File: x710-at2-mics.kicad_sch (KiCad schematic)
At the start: 1 part, among them U1 EZX710AT2_S_LMR5

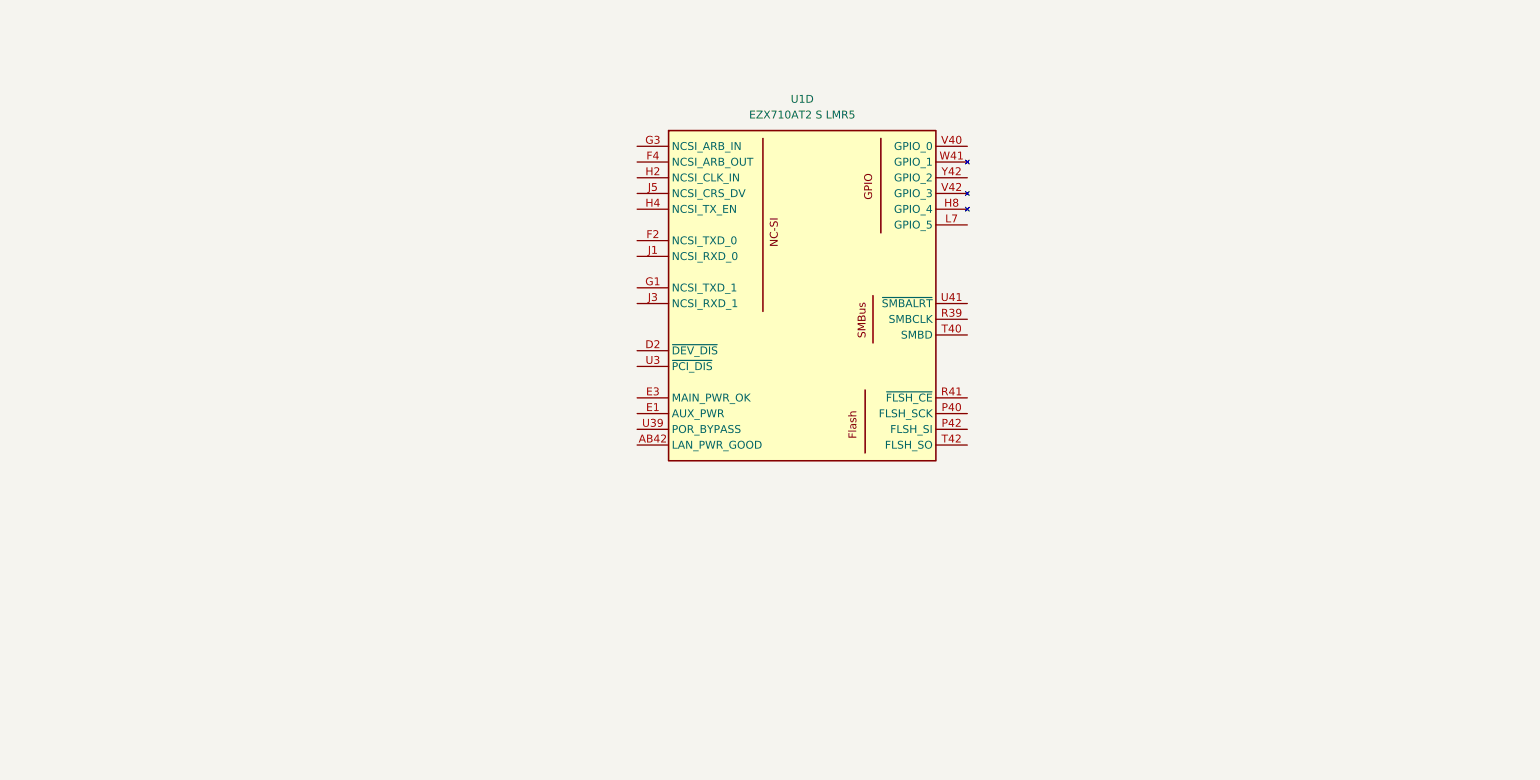
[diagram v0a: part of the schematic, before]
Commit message: [#80813] Add RJ45 connectors, add SMBus, FLASH SPI and misc
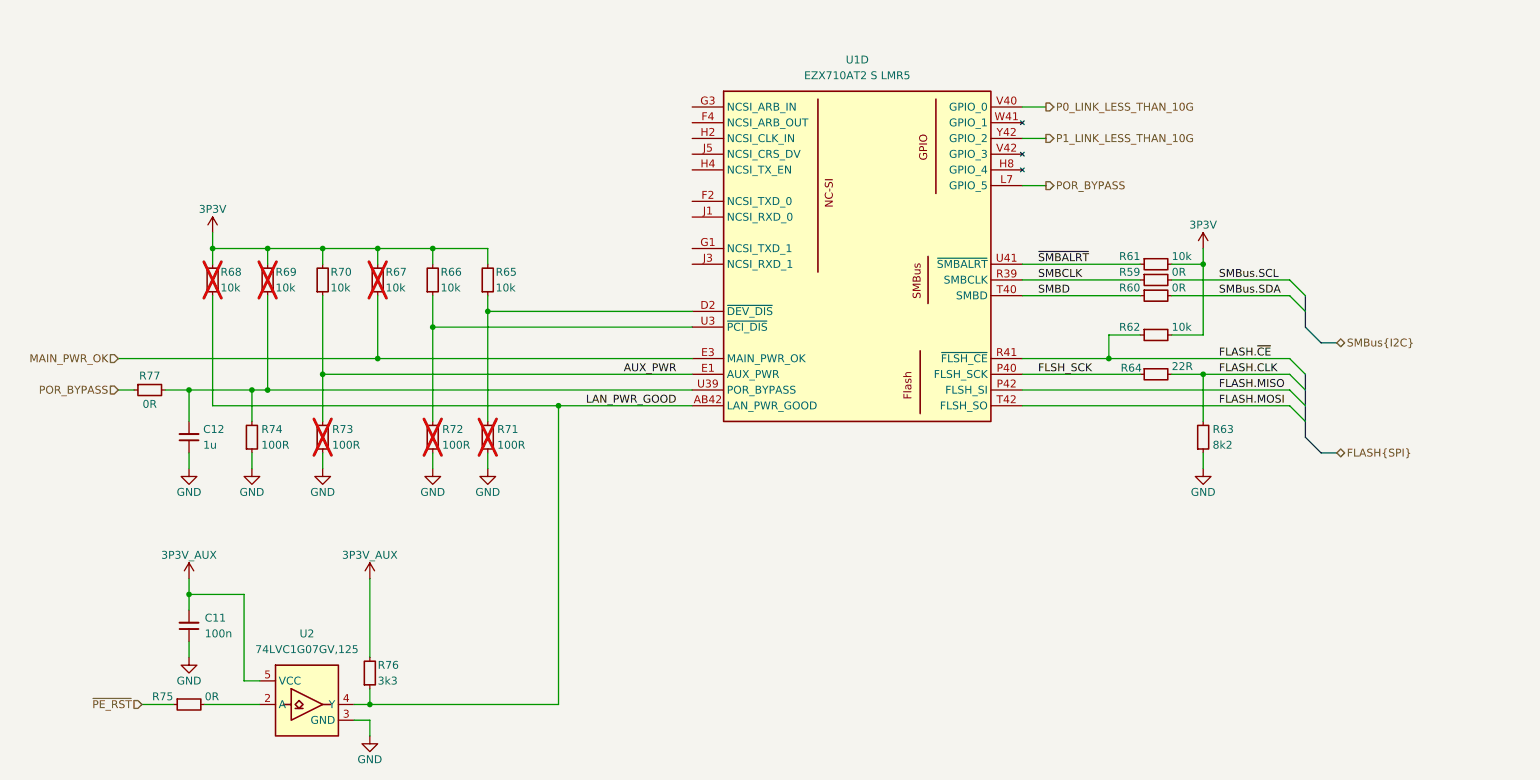
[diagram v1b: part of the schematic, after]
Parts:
- added C11: C_100n_16V_X7R_0402, antmicro-footprints:C_0402_1005Metric, symbol antmicroCapacitors0402:C_100n_16V_X7R_0402
- added C12: C_1u_16V_X7R_0603, antmicro-footprints:C_0603_1608Metric, symbol antmicroCapacitors0603:C_1u_16V_X7R_0603
- added R59, R60, R75, R77: R_0R_0402, antmicro-footprints:R_0402_1005Metric, symbol antmicroResistors0402:R_0R_0402
- added R61, R62, R65, R66, R67, R68, R69, R70: R_10k_0402, antmicro-footprints:R_0402_1005Metric, symbol antmicroResistors0402:R_10k_0402
- added R63: R_8k2_0402, antmicro-footprints:R_0402_1005Metric, symbol antmicroResistors0402:R_8k2_0402
- added R64: R_22R_0402, antmicro-footprints:R_0402_1005Metric, symbol antmicroResistors0402:R_22R_0402
- added R71, R72, R73, R74: R_100R_0402, antmicro-footprints:R_0402_1005Metric, symbol antmicroResistors0402:R_100R_0402
- added R76: R_3k3_0402, antmicro-footprints:R_0402_1005Metric, symbol antmicroResistors0402:R_3k3_0402
- added unit 6 of U1
- added U2: 74LVC1G07_SOT-753, antmicro-footprints:SOT-753, symbol antmicroLogicBuffersDriversReceiversTransceivers:74LVC1G07_SOT-753
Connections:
- net LAN_PWR_GOOD: now reaches U1.AB42 (LAN_PWR_GOOD)
- net LAN_PWR_GOOD: now also R68.1, R76.1, U2.4 (Y)
- net at U1.D2 (~{DEV_DIS}): now also R65.1, R71.2
- net AUX_PWR: now reaches U1.E1 (AUX_PWR)
- net AUX_PWR: now also R70.1, R73.2
- net MAIN_PWR_OK: now reaches U1.E3 (MAIN_PWR_OK)
- net MAIN_PWR_OK: now also R67.1
- net POR_BYPASS: now reaches U1.L7 (GPIO_5)
- net POR_BYPASS: now also R77.1
- net FLSH_SCK: now reaches U1.P40 (FLSH_SCK)
- net FLSH_SCK: now also R64.1
- net FLASH.MISO: now reaches U1.P42 (FLSH_SI)
- net SMBCLK: now reaches U1.R39 (SMBCLK)
- net SMBCLK: now also R59.1
- net FLASH.~{CE}: now reaches U1.R41 (~{FLSH_CE})
- net FLASH.~{CE}: now also R62.1
- net SMBD: now reaches U1.T40 (SMBD)
- net SMBD: now also R60.1
- net FLASH.MOSI: now reaches U1.T42 (FLSH_SO)
- net at U1.U3 (~{PCI_DIS}): now also R66.1, R72.2
- net at U1.U39 (POR_BYPASS): now also C12.2, R69.1, R74.2, R77.2
- net ~{SMBALRT}: now reaches U1.U41 (~{SMBALRT})
- net ~{SMBALRT}: now also R61.1
- net P0_LINK_LESS_THAN_10G: now reaches U1.V40 (GPIO_0)
- net P1_LINK_LESS_THAN_10G: now reaches U1.Y42 (GPIO_2)
- new net: R75.2, U2.2 (A)
- new net 3P3V: R61.2, R62.2, R65.2, R66.2, R67.2, R68.2, R69.2, R70.2
- new net 3P3V_AUX: C11.2, R76.2, U2.5 (VCC)
- new net FLASH.CLK: R63.2, R64.2
- new net GND: C11.1, C12.1, R63.1, R71.1, R72.1, R73.1, R74.1, U2.3 (GND)
- new net SMBus.SCL: R59.2
- new net SMBus.SDA: R60.2
- new net ~{PE_RST}: R75.1
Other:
- moved on the sheet: U1D

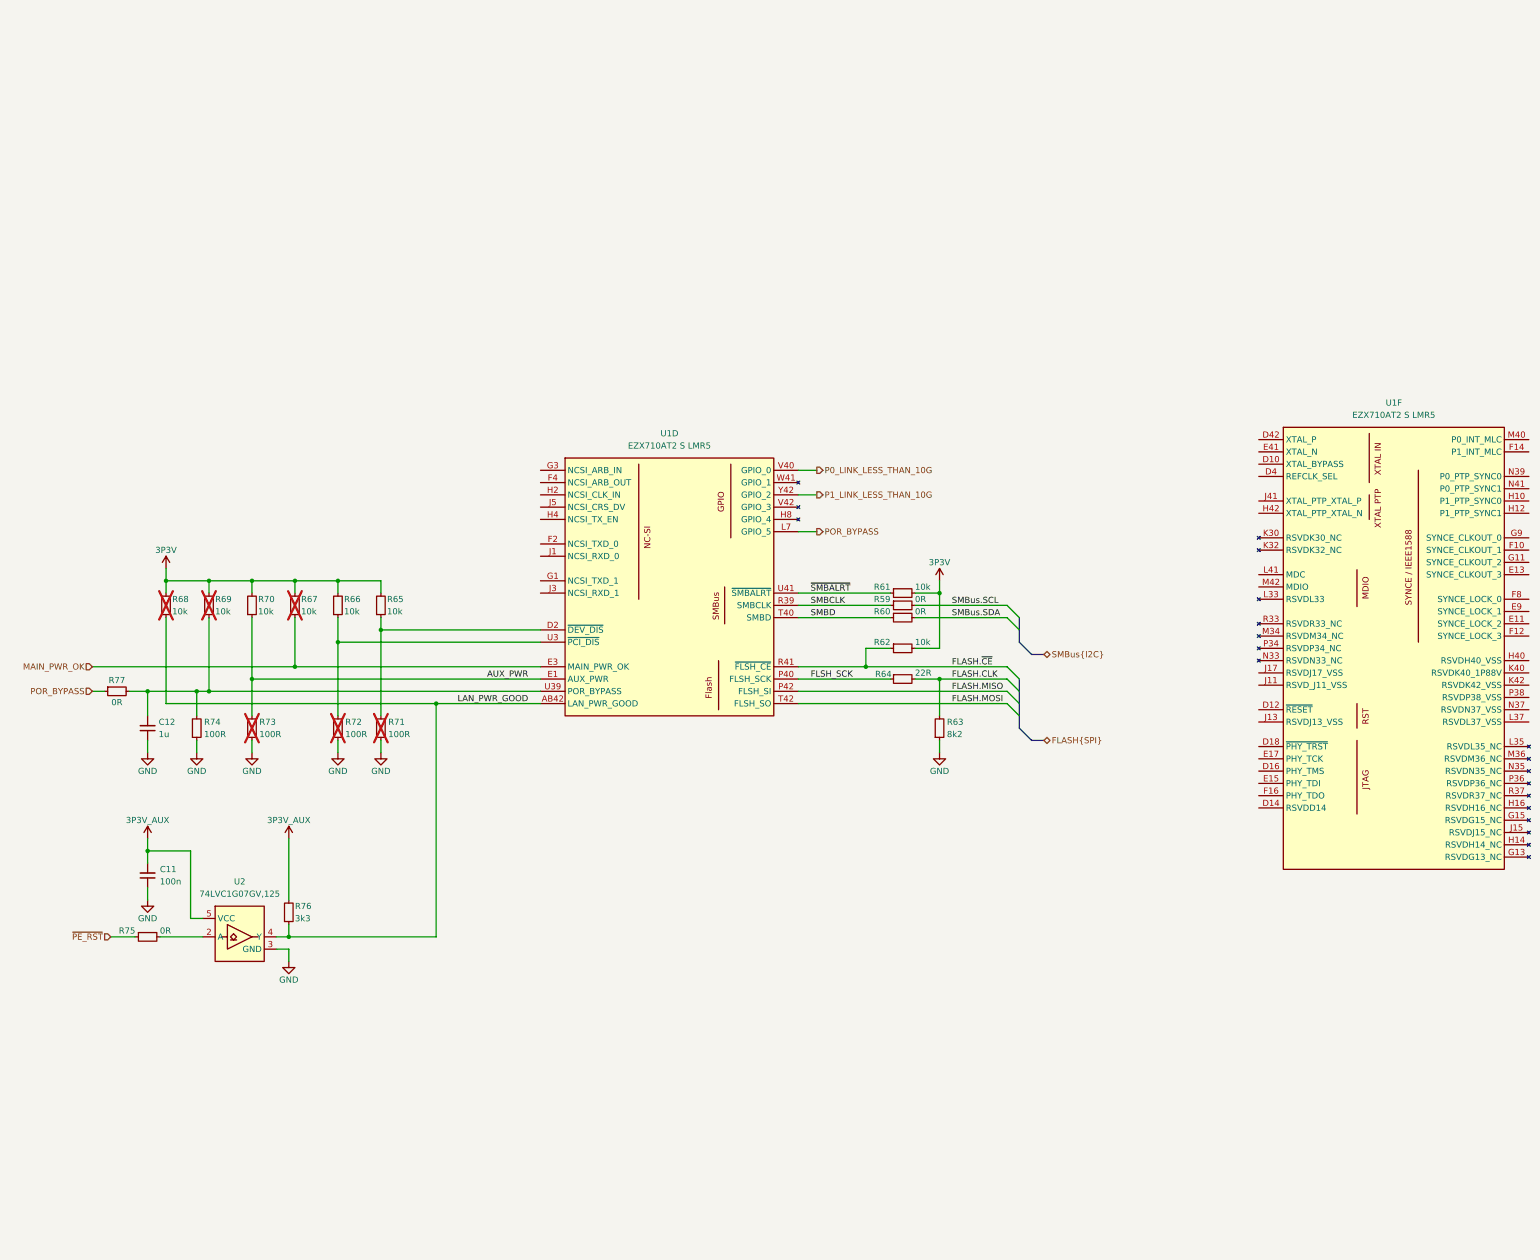
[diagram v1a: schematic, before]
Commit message: [#80813] Add NCSI bus
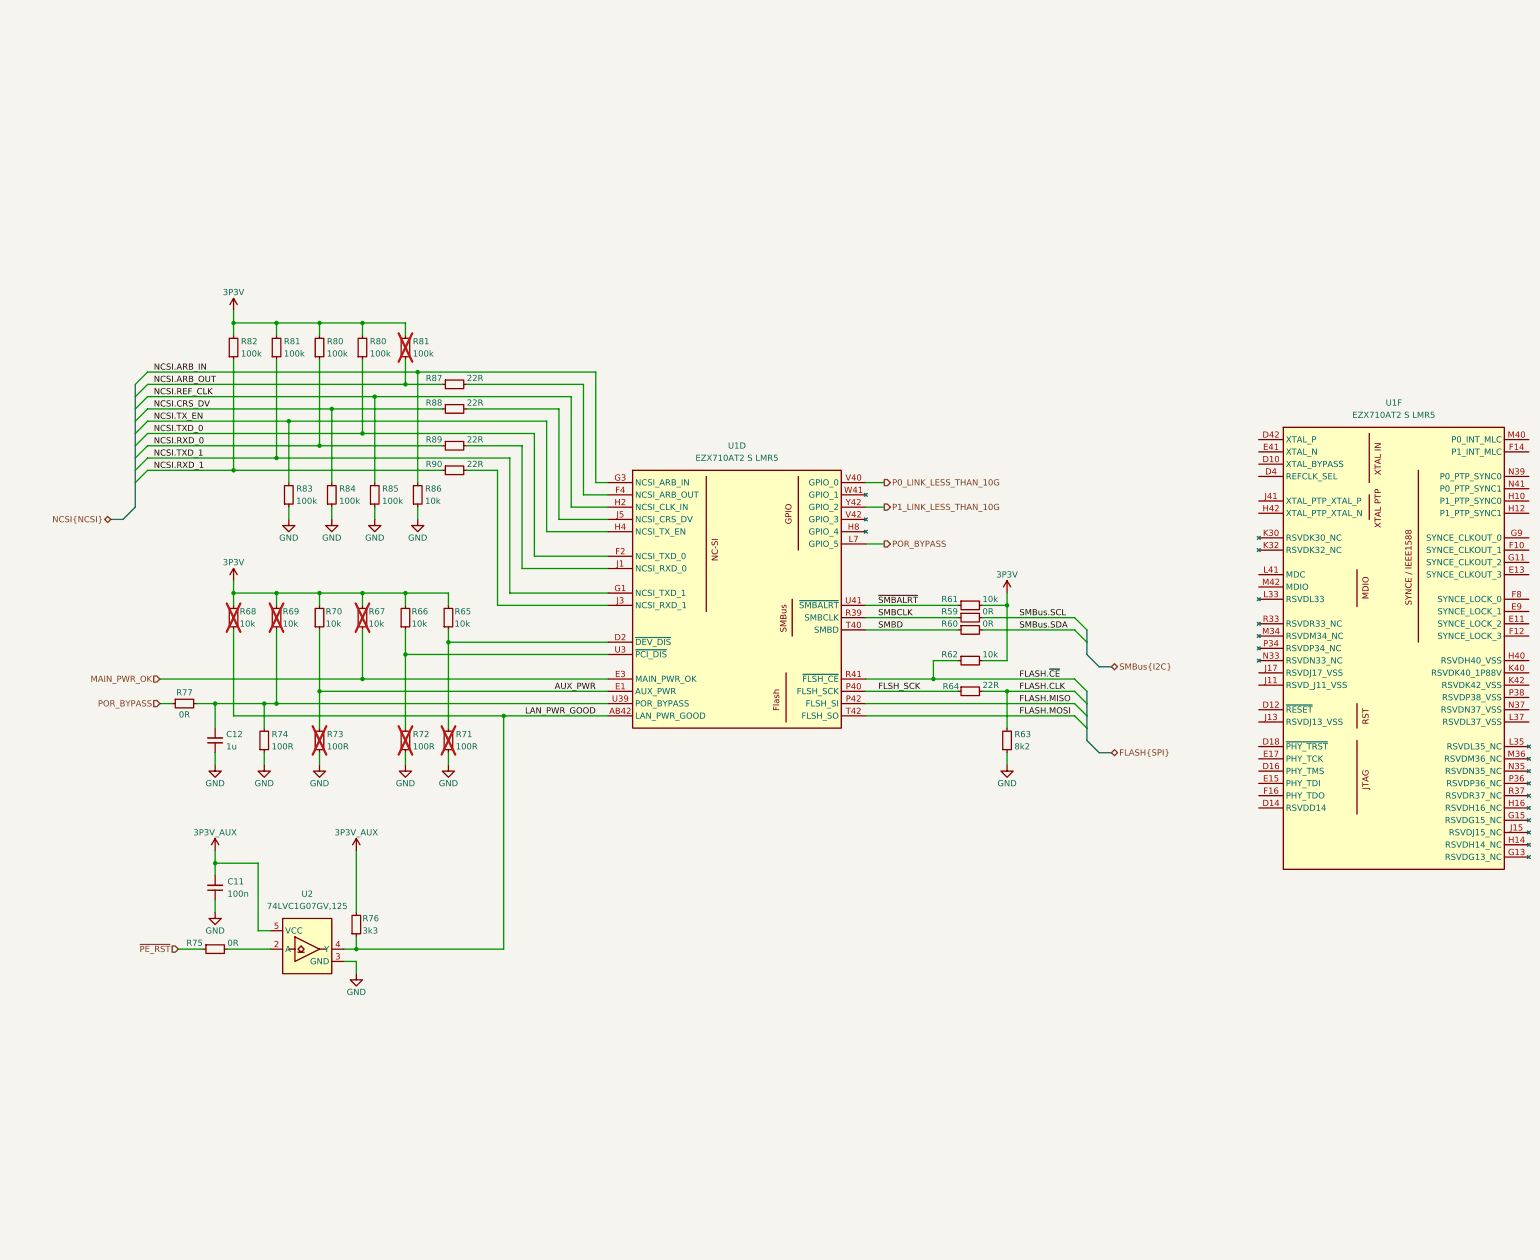
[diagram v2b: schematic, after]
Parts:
- added R80 (x2), R81 (x2), R82, R83, R84, R85: R_100k_0402, antmicro-footprints:R_0402_1005Metric, symbol antmicroResistors0402:R_100k_0402
- added R86: R_10k_0402, antmicro-footprints:R_0402_1005Metric, symbol antmicroResistors0402:R_10k_0402
- added R87, R88, R89, R90: R_22R_0402, antmicro-footprints:R_0402_1005Metric, symbol antmicroResistors0402:R_22R_0402
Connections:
- net 3P3V: now also R80.2, R80.2, R81.2, R81.2, R82.2
- net GND: now also R83.1, R84.1, R85.1, R86.1
- net NCSI.TXD_0: now reaches U1.F2 (NCSI_TXD_0)
- net NCSI.TXD_0: now also R80.1
- net at U1.F4 (NCSI_ARB_OUT): now also R87.2
- net NCSI.TXD_1: now reaches U1.G1 (NCSI_TXD_1)
- net NCSI.TXD_1: now also R81.1
- net NCSI.ARB_IN: now reaches U1.G3 (NCSI_ARB_IN)
- net NCSI.ARB_IN: now also R86.2
- net NCSI.REF_CLK: now reaches U1.H2 (NCSI_CLK_IN)
- net NCSI.REF_CLK: now also R85.2
- net NCSI.TX_EN: now reaches U1.H4 (NCSI_TX_EN)
- net NCSI.TX_EN: now also R83.2
- net at U1.J1 (NCSI_RXD_0): now also R89.2
- net at U1.J3 (NCSI_RXD_1): now also R90.2
- net at U1.J5 (NCSI_CRS_DV): now also R88.2
- new net NCSI.ARB_OUT: R81.1, R87.1
- new net NCSI.CRS_DV: R84.2, R88.1
- new net NCSI.RXD_0: R80.1, R89.1
- new net NCSI.RXD_1: R82.1, R90.1
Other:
- moved on the sheet: C11, C12, R59, R60, R61, R62, R63, R64, R65, R66, R67, R68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
